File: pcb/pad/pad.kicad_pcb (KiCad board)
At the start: 2 copper layers, 71 parts, among them J1 781710004, J2 512812498, J3 AVR-ISP-6, SW1 SW_Reset, U1 ATmega32U4-A, Y1 16mHz

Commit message: Update pcbs
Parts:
- removed J2: 512812498, Connector_FFC-FPC:Molex_502244-2430_1x24-1MP_P0.5mm_Horizontal
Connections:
- J1 pad MP: (no net) -> GND
- U1 pad 19: unconnected-(U1-PD1-Pad19) -> BRow0
- U1 pad 39: unconnected-(U1-PF4-Pad39) -> BCol2
- U1 pad 40: unconnected-(U1-PF1-Pad40) -> BCol1
- U1 pad 41: unconnected-(U1-PF0-Pad41) -> BCol0

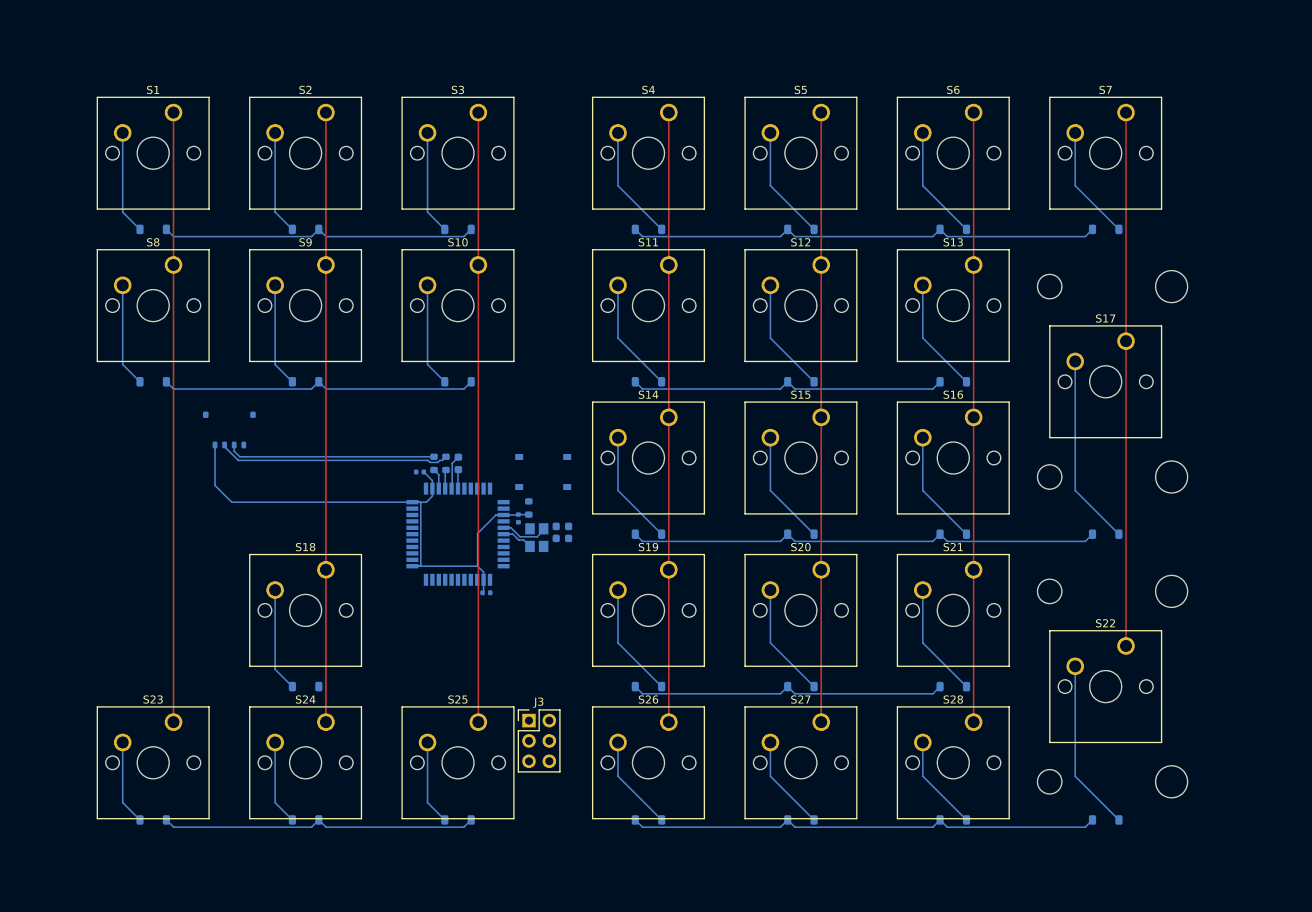
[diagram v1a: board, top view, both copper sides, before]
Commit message: Add FPC connector and restart board routing
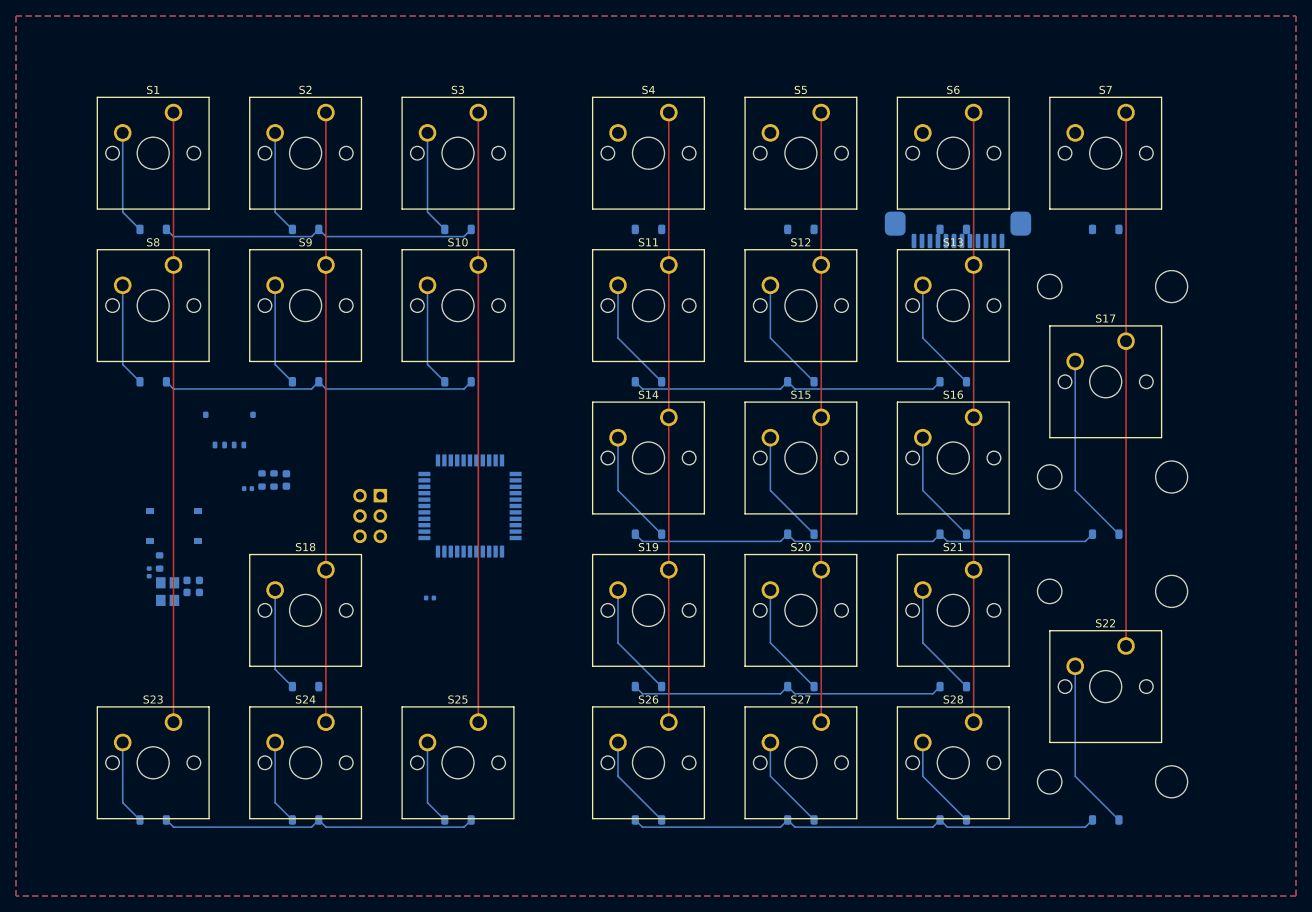
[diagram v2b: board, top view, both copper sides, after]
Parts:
- added J2: AFA07-S12FCA-00, Connector_FFC-FPC:JUSHUO_AFA07-S12FCA-00_1x12-1MP_P1.0mm_Horizontal, B.Cu at (169.7, 76.7)
- J3: moved to B.Cu
- moved C1 46.6 mm to (74.0, 124.0)
- moved C2 46.6 mm to (74.0, 122.5)
- moved C5 46.6 mm to (68.5, 121.5)
- moved R3 46.6 mm to (69.8, 120.2)
- moved Y1 46.6 mm to (70.8, 123.8)
- moved SW1 46.6 mm to (71.7, 115.7)
- moved J3 33.7 mm to (97.4, 111.9), turned to 180 degrees
- moved C3 21.6 mm to (85.7, 109.9)
- moved C4 21.6 mm to (80.9, 111.0)
- moved R1 21.6 mm to (84.2, 109.9)
- moved R2 21.6 mm to (82.7, 109.9)
- moved C6 7.08 mm to (103.7, 124.7)
- moved U1 3.83 mm to (108.7, 113.2), turned to 0 degrees
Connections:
- U1 pad 1: unconnected-(U1-PE6-Pad1) -> E1A
- U1 pad 32: unconnected-(U1-PC7-Pad32) -> E0A
- U1 pad 33: unconnected-(U1-~{HWB}/PE2-Pad33) -> E1B
- U1 pad 36: unconnected-(U1-PF7-Pad36) -> E2B
- U1 pad 37: unconnected-(U1-PF6-Pad37) -> E2A
- U1 pad 38: unconnected-(U1-PF5-Pad38) -> Col1
- U1 pad 8: Col1 -> SCK
- U1 pad 9: SCK -> E0B
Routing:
- net +5V: track 70.0 -> 0.00 mm
- net Row0: track 99.0 -> 39.6 mm
- net D+: track 28.8 -> 0.00 mm
- net D-: track 25.8 -> 0.00 mm
- net Net-(D6-A): track 14.3 -> 0.00 mm
- net Net-(D5-A): track 14.3 -> 0.00 mm
- net Net-(D4-A): track 14.3 -> 0.00 mm
- net Net-(D7-A): track 14.3 -> 0.00 mm
- net Net-(U1-XTAL2): track 6.00 -> 0.00 mm
- net GND: track 4.28 -> 0.00 mm
- net Net-(U1-XTAL1): track 3.93 -> 0.00 mm
- net Net-(U1-D-): track 2.57 -> 0.00 mm
- net Net-(U1-UCAP): track 2.40 -> 0.00 mm
- net Net-(U1-D+): track 2.37 -> 0.00 mm
- added copper zone on B.Cu, net GND
- added copper zone on F.Cu, net GND

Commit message: Update schematic and pcb
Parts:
- moved C4 23.9 mm to (101.9, 122.4), turned to 90 degrees
- moved R2 20.8 mm to (100.9, 119.9), turned to 0 degrees
- moved C6 19.9 mm to (97.9, 105.7)
- moved R1 18.8 mm to (100.9, 118.4), turned to 0 degrees
- moved SW1 16.2 mm to (87.7, 113.9)
- moved J1 9.58 mm to (81.2, 112.9), turned to 90 degrees
- moved U1 3.64 mm to (109.7, 116.7)
- moved J3 2.60 mm to (95.8, 109.8)
- moved C3 2.30 mm to (87.2, 108.2)
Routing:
- net MOSI: track 0.00 -> 12.2 mm
- net MISO: track 0.00 -> 9.30 mm
- net SCK: track 0.00 -> 9.24 mm
- net E0B: track 0.00 -> 6.58 mm, vias 0 -> 1
- net Net-(U1-D-): track 0.00 -> 2.58 mm
- net Net-(U1-D+): track 0.00 -> 2.29 mm
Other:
- board outline added: 138.1 x 95.2 mm

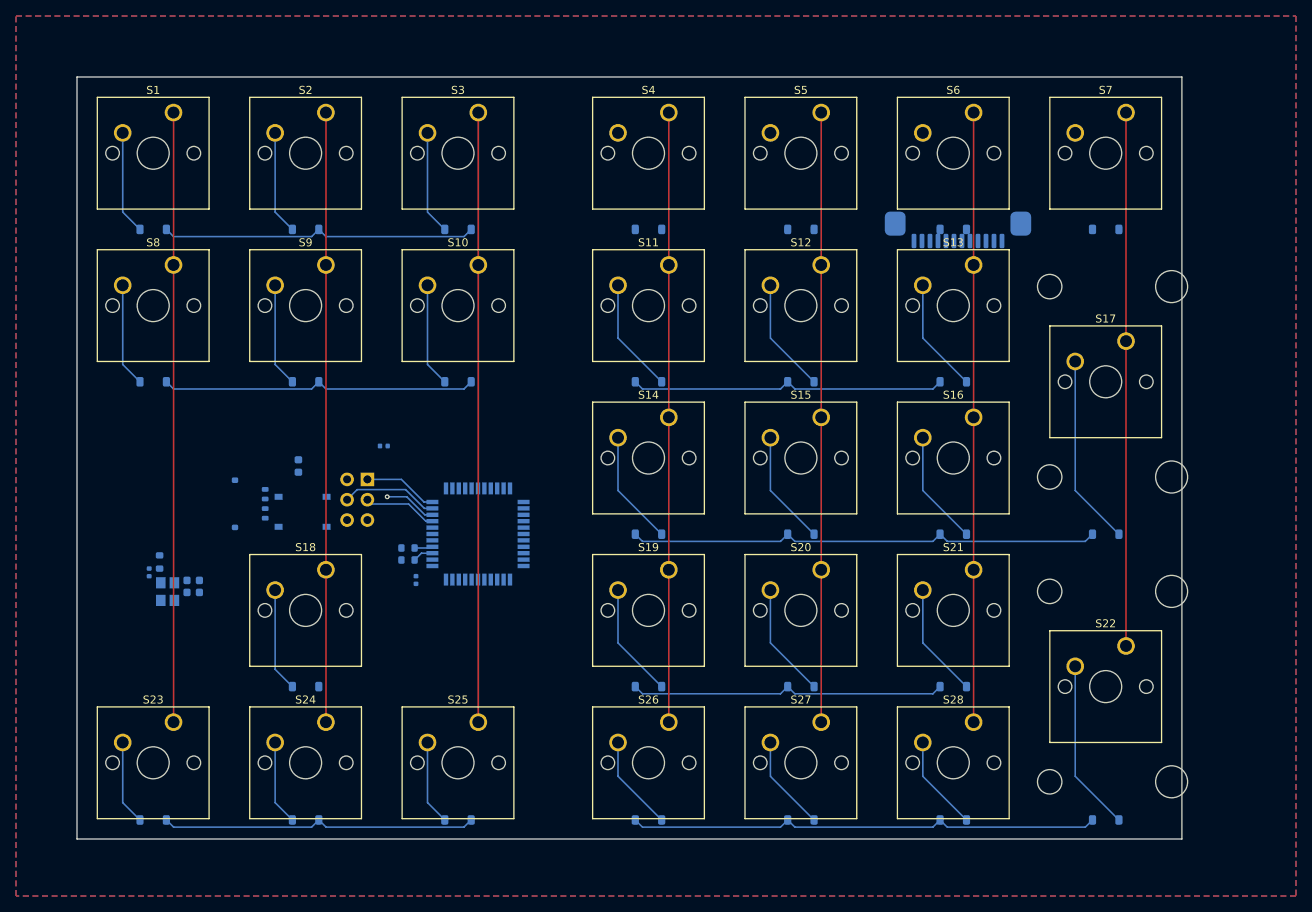
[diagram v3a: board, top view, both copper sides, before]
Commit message: Update FPC connectors
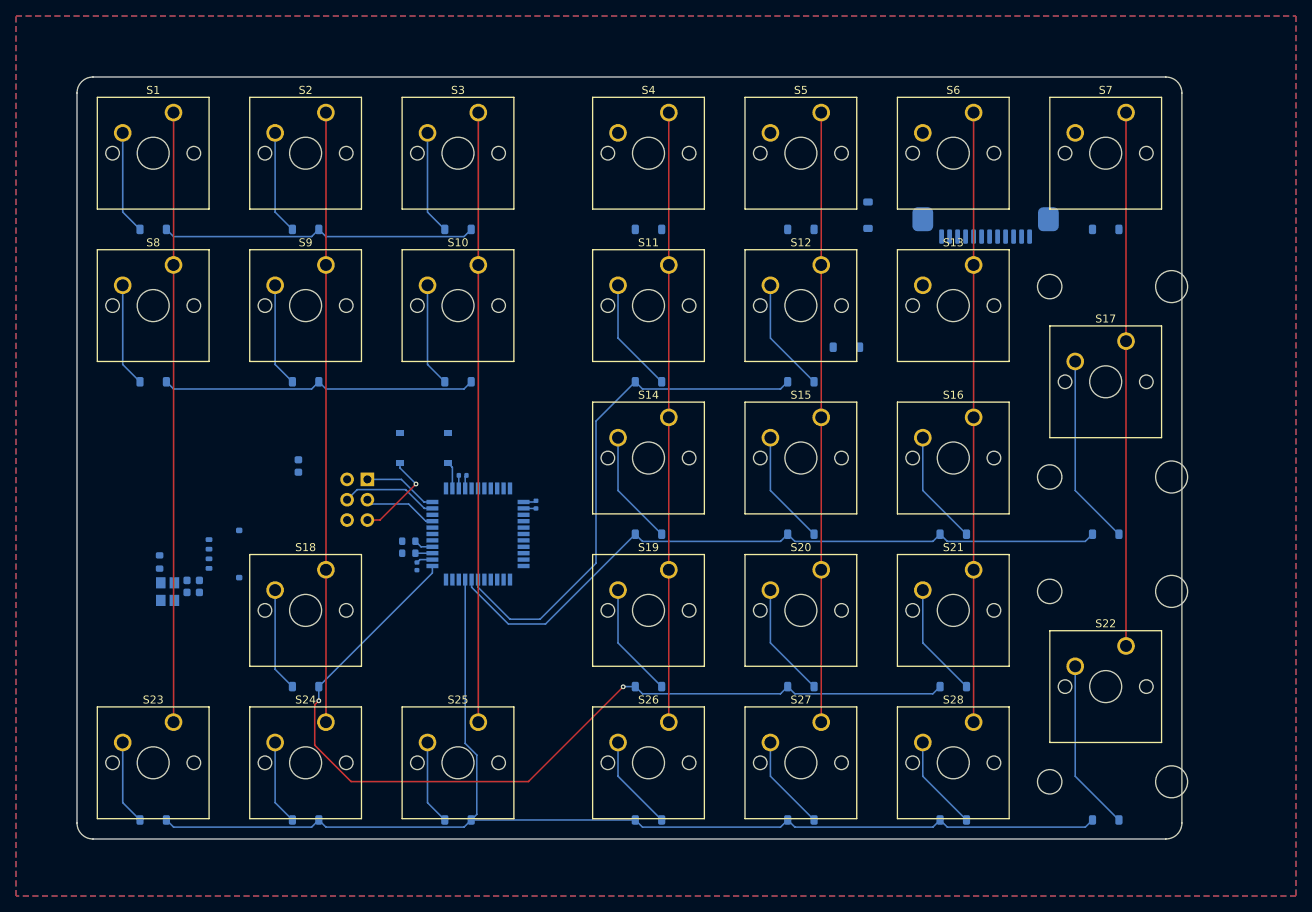
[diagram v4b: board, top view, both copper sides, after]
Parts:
- moved C5 41.0 mm to (107.7, 109.3), turned to 180 degrees
- moved C6 20.4 mm to (116.9, 113.0), turned to -90 degrees
- moved SW1 17.1 mm to (102.9, 105.9)
- moved D13 14.0 mm to (155.7, 93.3)
- moved D6 10.8 mm to (158.4, 76.8), turned to 90 degrees
- moved J1 7.08 mm to (77.9, 119.2), turned to -90 degrees
- moved J2 3.49 mm to (173.1, 76.1)
- moved C4 1.71 mm to (102.0, 120.7)
- moved R1 0.86 mm to (101.0, 117.5)
- moved R2 0.86 mm to (101.0, 119.0)
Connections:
- U1 pad 1: E1A -> Row3
- U1 pad 12: Col2 -> unconnected-(U1-PB7-Pad12)
- U1 pad 18: Row0 -> unconnected-(U1-PD0-Pad18)
- U1 pad 19: BRow0 -> unconnected-(U1-PD1-Pad19)
- U1 pad 20: Col4 -> unconnected-(U1-PD2-Pad20)
- U1 pad 21: Row4 -> unconnected-(U1-PD3-Pad21)
- U1 pad 22: Row3 -> unconnected-(U1-PD5-Pad22)
- U1 pad 25: Row2 -> unconnected-(U1-PD4-Pad25)
- U1 pad 26: Row1 -> unconnected-(U1-PD6-Pad26)
- U1 pad 27: Col3 -> unconnected-(U1-PD7-Pad27)
- U1 pad 28: Col6 -> unconnected-(U1-PB4-Pad28)
- U1 pad 29: Col5 -> unconnected-(U1-PB5-Pad29)
- U1 pad 30: Col0 -> unconnected-(U1-PB6-Pad30)
- U1 pad 31: Row5 -> unconnected-(U1-PC6-Pad31)
- U1 pad 32: E0A -> unconnected-(U1-PC7-Pad32)
- U1 pad 33: E1B -> unconnected-(U1-~{HWB}/PE2-Pad33)
- U1 pad 36: E2B -> unconnected-(U1-PF7-Pad36)
- U1 pad 37: E2A -> unconnected-(U1-PF6-Pad37)
- U1 pad 38: Col1 -> E0B
- U1 pad 39: BCol2 -> Row1
- U1 pad 40: BCol1 -> Row2
- U1 pad 41: BCol0 -> Row4
- U1 pad 9: E0B -> unconnected-(U1-PB1-Pad9)
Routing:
- net Row3: track 39.6 -> 115.0 mm, vias 0 -> 2
- net Row4: track 99.0 -> 150.4 mm
- net Row2: track 59.4 -> 87.4 mm
- net Row1: track 79.2 -> 104.4 mm
- net RESET: track 0.00 -> 14.8 mm, vias 0 -> 1
- net Net-(D13-A): track 14.3 -> 0.00 mm
- net E0B: track 6.58 -> 0.00 mm, vias 1 -> 0
- net +5V: track 0.00 -> 5.26 mm
- net GND: track 0.00 -> 3.31 mm
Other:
- outline, holes or cut-outs redrawn
